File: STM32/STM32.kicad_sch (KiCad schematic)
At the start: 5 parts, among them SW1 SW_Push, U1 STM32F091RCTx

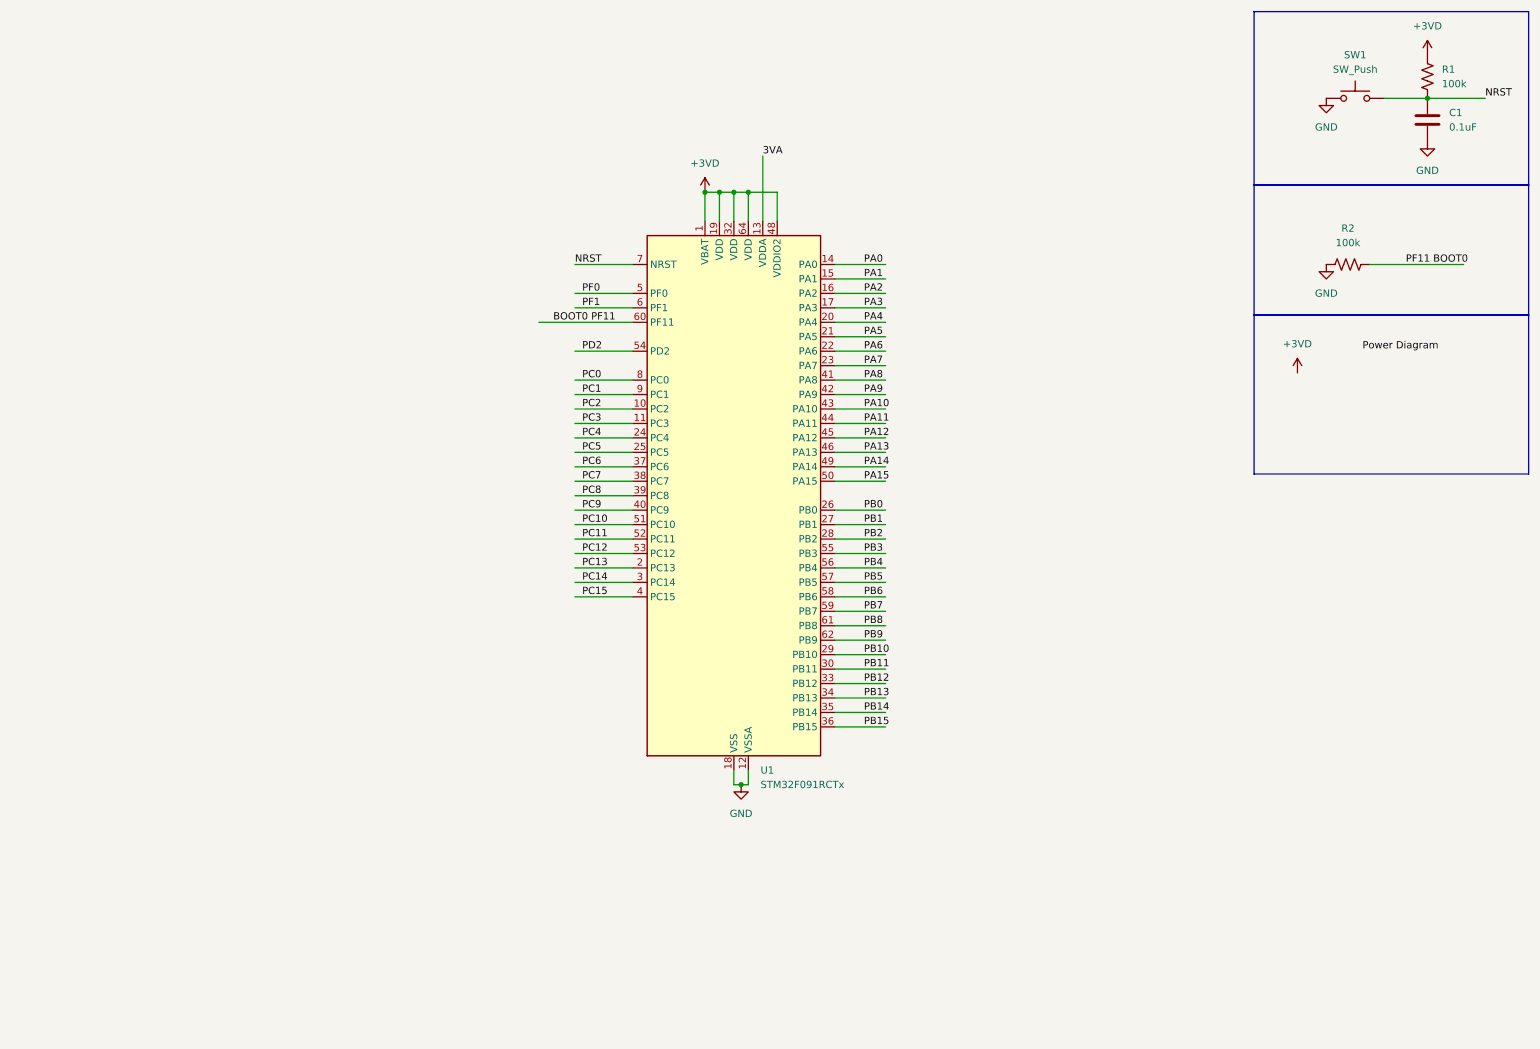
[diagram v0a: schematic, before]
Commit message: Add files via upload
adjusted schematic
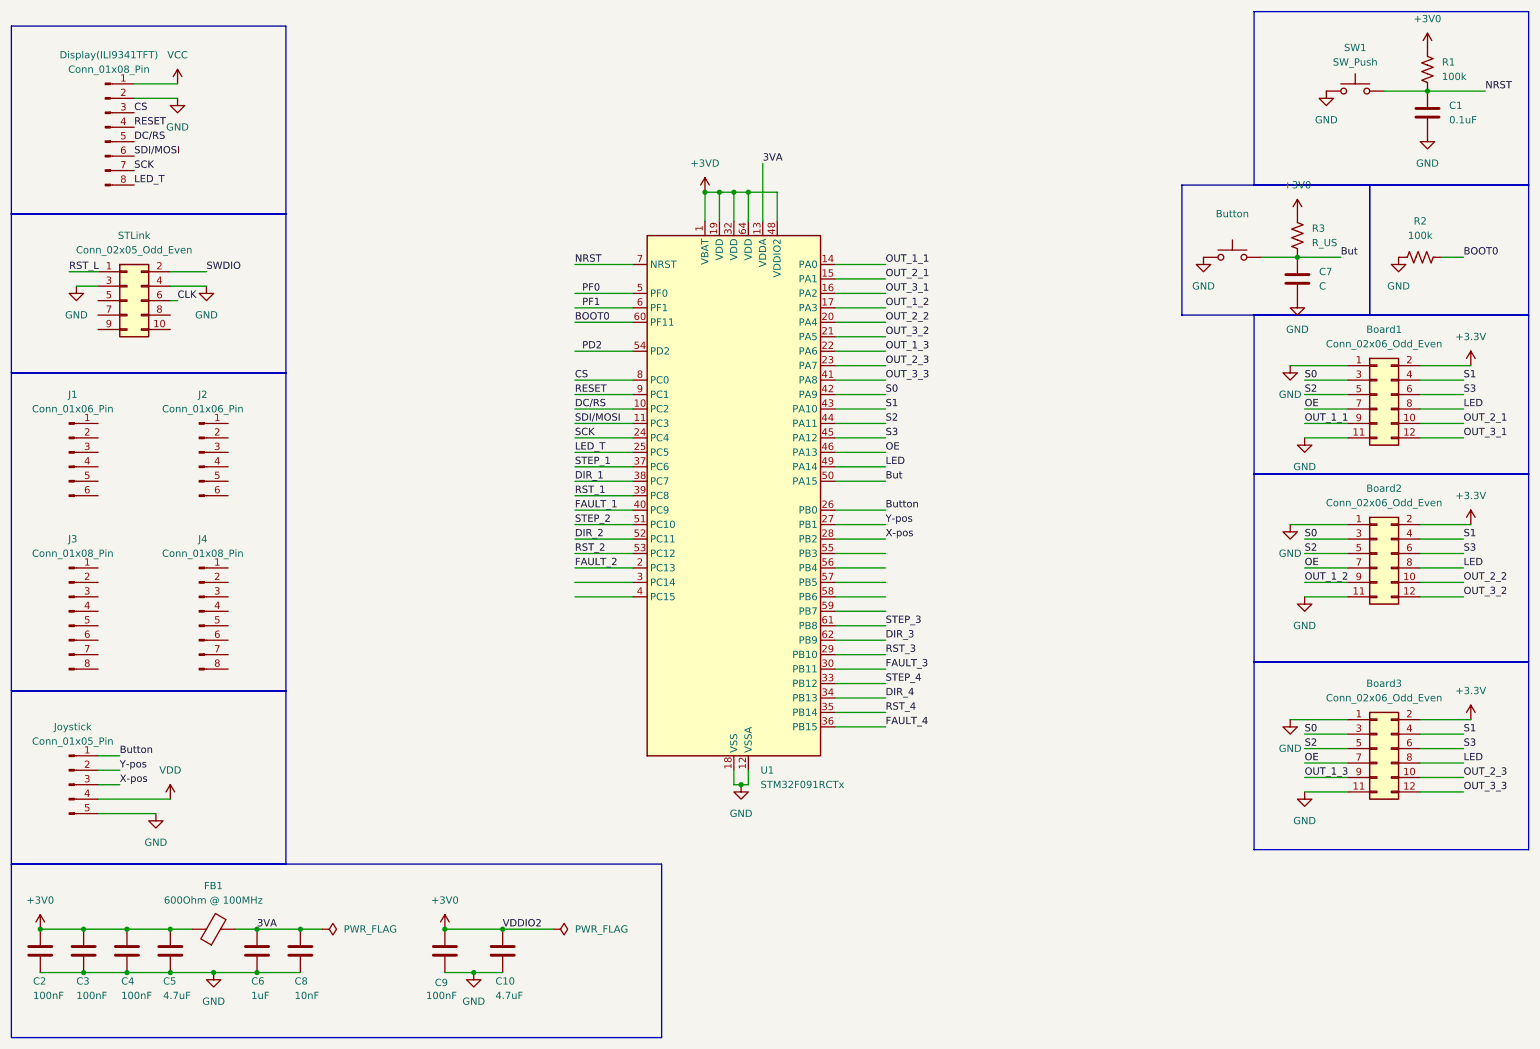
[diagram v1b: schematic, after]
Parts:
- added Board1, Board2, Board3: Conn_02x06_Odd_Even, symbol Connector_Generic:Conn_02x06_Odd_Even
- added Button: ~, symbol Switch:SW_Push
- added C10, C5: 4.7uF, symbol Device:C
- added C2, C3, C4, C9: 100nF, symbol Device:C
- added C6: 1uF, symbol Device:C
- added C7: C, symbol Device:C
- added C8: 10nF, symbol Device:C
- added Display(ILI9341TFT), J3, J4: Conn_01x08_Pin, symbol Connector:Conn_01x08_Pin
- added FB1: 600Ohm @ 100MHz, symbol Device:FerriteBead
- added J1, J2: Conn_01x06_Pin, symbol Connector:Conn_01x06_Pin
- added Joystick: Conn_01x05_Pin, symbol Connector:Conn_01x05_Pin
- added R3: R_US, symbol Device:R_US
- added STLink: Conn_02x05_Odd_Even, symbol Connector_Generic:Conn_02x05_Odd_Even
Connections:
- net PF11 BOOT0 is gone; now on net BOOT0: R2.2
- net +3VD: no longer R1.1
- net 3VA: now also C6.1, C8.1, FB1.2
- net GND: now also Board1.1 (Pin_1), Board1.11 (Pin_11), Board2.1 (Pin_1), Board2.11 (Pin_11), Board3.1 (Pin_1), Board3.11 (Pin_11), Button.1, C10.2, C2.2, C3.2, C4.2, C5.2, C6.2, C7.2, C8.2, C9.2, Display(ILI9341TFT).2 (Pin_2), Joystick.5 (Pin_5), STLink.3 (Pin_3), STLink.4 (Pin_4)
- net BOOT0 PF11 renamed BOOT0
- net PA0 renamed OUT_1_1
- net OUT_1_1: now also Board1.9 (Pin_9)
- net PA1 renamed OUT_2_1
- net OUT_2_1: now also Board1.10 (Pin_10)
- net PA10 renamed S1
- net S1: now also Board1.4 (Pin_4), Board2.4 (Pin_4), Board3.4 (Pin_4)
- net PA11 renamed S2
- net S2: now also Board1.5 (Pin_5), Board2.5 (Pin_5), Board3.5 (Pin_5)
- net PA12 renamed S3
- net S3: now also Board1.6 (Pin_6), Board2.6 (Pin_6), Board3.6 (Pin_6)
- net PA13 renamed OE
- net OE: now also Board1.7 (Pin_7), Board2.7 (Pin_7), Board3.7 (Pin_7)
- net PA14 renamed LED
- net LED: now also Board1.8 (Pin_8), Board2.8 (Pin_8), Board3.8 (Pin_8)
- net PA15 renamed But
- net But: now also Button.2, C7.1, R3.2
- net PA2 renamed OUT_3_1
- net OUT_3_1: now also Board1.12 (Pin_12)
- net PA3 renamed OUT_1_2
- net OUT_1_2: now also Board2.9 (Pin_9)
- net PA4 renamed OUT_2_2
- net OUT_2_2: now also Board2.10 (Pin_10)
- net PA5 renamed OUT_3_2
- net OUT_3_2: now also Board2.12 (Pin_12)
- net PA6 renamed OUT_1_3
- net OUT_1_3: now also Board3.9 (Pin_9)
- net PA7 renamed OUT_2_3
- net OUT_2_3: now also Board3.10 (Pin_10)
- net PA8 renamed OUT_3_3
- net OUT_3_3: now also Board3.12 (Pin_12)
- net PA9 renamed S0
- net S0: now also Board1.3 (Pin_3), Board2.3 (Pin_3), Board3.3 (Pin_3)
- net PB0 renamed Button
- net Button: now also Joystick.1 (Pin_1)
- net PB1 renamed Y-pos
- net Y-pos: now also Joystick.2 (Pin_2)
- net PB10 renamed RST_3
- net PB11 renamed FAULT_3
- net PB12 renamed STEP_4
- net PB13 renamed DIR_4
- net PB14 renamed RST_4
- net PB15 renamed FAULT_4
- net PB2 renamed X-pos
- net X-pos: now also Joystick.3 (Pin_3)
- net PB3: no longer names the net of U1.55 (PB3)
- net PB4: no longer names the net of U1.56 (PB4)
- net PB5: no longer names the net of U1.57 (PB5)
- net PB6: no longer names the net of U1.58 (PB6)
- net PB7: no longer names the net of U1.59 (PB7)
- net PB8 renamed STEP_3
- net PB9 renamed DIR_3
- net PC0 renamed CS
- net CS: now also Display(ILI9341TFT).3 (Pin_3)
- net PC1 renamed RESET
- net RESET: now also Display(ILI9341TFT).4 (Pin_4)
- net PC10 renamed STEP_2
- net PC11 renamed DIR_2
- net PC12 renamed RST_2
- net PC13 renamed FAULT_2
- net PC14: no longer names the net of U1.3 (PC14)
- net PC15: no longer names the net of U1.4 (PC15)
- net PC2 renamed DC/RS
- net DC/RS: now also Display(ILI9341TFT).5 (Pin_5)
- net PC3 renamed SDI/MOSI
- net SDI/MOSI: now also Display(ILI9341TFT).6 (Pin_6)
- net PC4 renamed SCK
- net SCK: now also Display(ILI9341TFT).7 (Pin_7)
- net PC5 renamed LED_T
- net LED_T: now also Display(ILI9341TFT).8 (Pin_8)
- net PC6 renamed STEP_1
- net PC7 renamed DIR_1
- net PC8 renamed RST_1
- net PC9 renamed FAULT_1
- new net +3.3V: Board1.2 (Pin_2), Board2.2 (Pin_2), Board3.2 (Pin_2)
- new net +3V0: C10.1, C2.1, C3.1, C4.1, C5.1, C9.1, FB1.1, R1.1, R3.1
- new net CLK: STLink.6 (Pin_6)
- new net RST_L: STLink.1 (Pin_1)
- new net SWDIO: STLink.2 (Pin_2)
- new net VCC: Display(ILI9341TFT).1 (Pin_1)
- new net VDD: Joystick.4 (Pin_4)
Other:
- moved on the sheet: C1, R1, R2, SW1

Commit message: Add files via upload
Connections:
- net +3V0: no longer C10.1, C9.1
- net +3VD: now also C10.1, C9.1
- net 3VA renamed VDDA
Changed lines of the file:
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@@
 	)
 	(junction
+		(at 147.32 44.45)
+		(diameter 0)
+		(color 0 0 0 0)
+	)
+	(junction
 		(at 17.78 173.99)
 		(diameter 0)
@@
 	(wire
 		(pts
+			(xy 147.32 41.91) (xy 147.32 44.45)
+		)
+		(stroke
+			(width 0)
+			(type default)
+		)
+	)
+	(wire
+		(pts
 			(xy 33.02 181.61) (xy 40.64 181.61)
 		)
@@
 	(wire
 		(pts
-			(xy 147.32 49.53) (xy 147.32 44.45)
-		)
-		(stroke
-			(width 0)
-			(type default)
-		)
-	)
-	(wire
-		(pts
 			(xy 140.97 148.59) (xy 142.24 148.59)
 		)
@@
 	(wire
 		(pts
+			(xy 147.32 44.45) (xy 147.32 49.53)
+		)
+		(stroke
+			(width 0)
+			(type default)
+		)
+	)
+	(wire
+		(pts
 			(xy 111.76 110.49) (xy 121.92 110.49)
 		)
@@
 		)
 	)
-	(label "3VA"
-		(at 144.78 39.37 0)
-		(effects
-			(font
-				(size 1.27 1.27)
-			)
-			(justify left bottom)
-		)
-	)
 	(label "NRST"
 		(at 111.76 57.15 0)
@@
 		)
 	)
-	(label "3VA"
-		(at 55.88 173.99 0)
-		(effects
-			(font
-				(size 1.27 1.27)
-			)
-			(justify left bottom)
-		)
-	)
 	(label "S2"
 		(at 240.03 107.95 0)
@@
 		)
 	)
-	(label "VDDIO2"
-		(at 99.06 173.99 0)
-		(effects
-			(font
-				(size 1.27 1.27)
-			)
-			(justify left bottom)
-		)
-	)
 	(label "DC{slash}RS"
 		(at 34.29 35.56 0)
@@
 		(on_board yes)
 		(dnp no)
-		(fields_autoplaced yes)
 		(property "Reference" "#PWR026"
 			(at 88.9 177.8 0)
@@
 			)
 		)
-		(property "Value" "+3V0"
-			(at 88.9 168.91 0)
+		(property "Value" "VDDIO2"
+			(at 86.614 169.672 0)
 			(effects
 				(font
 					(size 1.27 1.27)
 				)
+				(justify left)
 			)
 		)
@@
 	)
 	(symbol
+		(lib_id "power:VDD")
+		(at 144.78 39.37 0)
+		(unit 1)
+		(exclude_from_sim no)
+		(in_bom yes)
+		(on_board yes)
+		(dnp no)
+		(fields_autoplaced yes)
+		(property "Reference" "#PWR029"
+			(at 144.78 43.18 0)
+			(effects
+				(font
+					(size 1.27 1.27)
+				)
+				(hide yes)
+			)
+		)
+		(property "Value" "VDDA"
+			(at 144.78 34.29 0)
+			(effects
+				(font
+					(size 1.27 1.27)
+				)
+			)
+		)
+		(property "Footprint" ""
+			(at 144.78 39.37 0)
+			(effects
+				(font
+					(size 1.27 1.27)
+				)
+				(hide yes)
+			)
+		)
+		(property "Datasheet" ""
+			(at 144.78 39.37 0)
+			(effects
+				(font
+					(size 1.27 1.27)
+				)
+				(hide yes)
+			)
+		)
+		(property "Description" "Power symbol creates a global label with name \"VDD\""
+			(at 144.78 39.37 0)
+			(effects
+				(font
+					(size 1.27 1.27)
+				)
+				(hide yes)
+			)
+		)
+		(pin "1"
+		)
+		(instances
+			(project ""
+				(path "/4c59bd81-5775-41d0-8b13-aaa71c70e7bc"
+					(reference "#PWR029")
+					(unit 1)
+				)
+			)
+		)
+	)
+	(symbol
 		(lib_id "power:GND")
 		(at 48.26 181.61 0)
@@
 	)
 	(symbol
+		(lib_id "power:VDD")
+		(at 147.32 41.91 0)
+		(unit 1)
+		(exclude_from_sim no)
+		(in_bom yes)
+		(on_board yes)
+		(dnp no)
+		(property "Reference" "#PWR031"
+			(at 147.32 45.72 0)
+			(effects
+				(font
+					(size 1.27 1.27)
+				)
+				(hide yes)
+			)
+		)
+		(property "Value" "VDDIO2"
+			(at 151.892 39.878 0)
+			(effects
+				(font
+					(size 1.27 1.27)
+				)
+			)
+		)
+		(property "Footprint" ""
+			(at 147.32 41.91 0)
+			(effects
+				(font
+					(size 1.27 1.27)
+				)
+				(hide yes)
+			)
+		)
+		(property "Datasheet" ""
+			(at 147.32 41.91 0)
+			(effects
+				(font
+					(size 1.27 1.27)
+				)
+				(hide yes)
+			)
+		)
+		(property "Description" "Power symbol creates a global label with name \"VDD\""
+			(at 147.32 41.91 0)
+			(effects
+				(font
+					(size 1.27 1.27)
+				)
+				(hide yes)
+			)
+		)
+		(pin "1"
+		)
+		(instances
+			(project ""
+				(path "/4c59bd81-5775-41d0-8b13-aaa71c70e7bc"
+					(reference "#PWR031")
+					(unit 1)
+				)
+			)
+		)
+	)
+	(symbol
 		(lib_id "power:+3V0")
 		(at 261.62 19.05 0)
@@
 		(on_board yes)
 		(dnp no)
-		(fields_autoplaced yes)
 		(property "Reference" "FB1"
-			(at 48.2092 166.37 90)
+			(at 41.91 165.608 90)
 			(effects
 				(font
@@
 		)
 		(property "Value" "600Ohm @ 100MHz"
-			(at 48.2092 168.91 90)
+			(at 41.91 168.148 90)
 			(effects
 				(font
@@
 					(unit 1)
 				)
+			)
+		)
+	)
+	(symbol
+		(lib_id "power:VDD")
+		(at 55.88 173.99 0)
+		(unit 1)
+		(exclude_from_sim no)
+		(in_bom yes)
+		(on_board yes)
+		(dnp no)
+		(property "Reference" "#PWR030"
+			(at 55.88 177.8 0)
+			(effects
+				(font
+					(size 1.27 1.27)
+				)
+				(hide yes)
+			)
+		)
+		(property "Value" "VDDA"
+			(at 57.15 170.434 0)
+			(effects
+				(font
+					(size 1.27 1.27)
+				)
+			)
+		)
+		(property "Footprint" ""
+			(at 55.88 173.99 0)
+			(effects
+				(font
+					(size 1.27 1.27)
+				)
+				(hide yes)
+			)
+		)
+		(property "Datasheet" ""
+			(at 55.88 173.99 0)
+			(effects
+				(font
+					(size 1.27 1.27)
+				)
+				(hide yes)
+			)
+		)
+		(property "Description" "Power symbol creates a global label with name \"VDD\""
+			(at 55.88 173.99 0)
+			(effects
+				(font
+					(size 1.27 1.27)
+				)
+				(hide yes)
+			)
+		)
+		(pin "1"
+		)
+		(instances
+			(project "STM32"
+				(path "/4c59bd81-5775-41d0-8b13-aaa71c70e7bc"
+					(reference "#PWR030")
+					(unit 1)
+				)

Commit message: Add files via upload
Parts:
- Board1, Board2, Board3: footprint (none) -> Connector_PinHeader_1.00mm:PinHeader_2x06_P1.00mm_Vertical
- Button1: renamed from Button; footprint (none) -> Button_Switch_SMD:SW_SPST_TL3342
- C1, C10, C2, C3, C4, C5, C6, C7, C8, C9: footprint (none) -> Capacitor_SMD:C_0603_1608Metric
- Display(ILI9341TFT)1: renamed from Display(ILI9341TFT); footprint (none) -> Connector_PinHeader_1.00mm:PinHeader_1x08_P1.00mm_Vertical
- FB1, R1, R2, R3: footprint (none) -> Resistor_SMD:R_0603_1608Metric
- J1, J2: footprint (none) -> Connector_PinHeader_1.00mm:PinHeader_1x06_P1.00mm_Vertical
- J3, J4: footprint (none) -> Connector_PinHeader_1.00mm:PinHeader_1x08_P1.00mm_Vertical
- Joystick1: renamed from Joystick; footprint (none) -> Connector_PinHeader_1.00mm:PinHeader_1x05_P1.00mm_Vertical
- STLink1: renamed from STLink; footprint (none) -> Connector_PinHeader_1.00mm:PinHeader_2x05_P1.00mm_Vertical
- SW1: footprint (none) -> Button_Switch_SMD:SW_SPST_TL3342
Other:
- moved on the sheet: Button1, C7, R3
